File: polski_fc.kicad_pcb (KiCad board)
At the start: 8 copper layers, 37 x 37 mm, 157 parts, among them J2 JST-SH 1x08, J3 Digital_VTX_Connector, J4 UJ20-C-H-G-SMT-5-P16-TR, P1 4V5, P10 R1, P11 +, P12 C, P13 R5, P14 M1, P15 M2, P16 M3, P17 M4, P18 G, P19 5V, P2 G, P20 G, P21 VI, P22 5V, P23 G, P24 T5, P25 R5, P26 5V, P27 LED, P28 G, P29 5V, P3 SCL, P30 -B, P31 G, P32 T2, P33 R2, P34 R1, P35 G, P36 G, P37 9V, P38 5V, P39 G, P4 SDA, P40 5V, P41 G, P42 T5, P43 T5, P5 T3, P6 R3, P7 4V5, P8 G, P9 T1, Q1 NX138AKMYL, SW1 BOOT, U1 STM32G473RET6, U2 LMR33630CRNXR, U3 LMR33630CRNXR, U4 NCP187AMT330TAG, U5 TCR3RM33A, U6 ICM-42688-P, U7 DPS368XTSA1, U8 W25Q128JVPIQ, U9 STM32G431KBU6, Y1 8MHz

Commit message: Added silkscren
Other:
- board text added: "3V3"
- board text added: "4V5"
- board text added: "5V"
- board text added: "9V"
- board text added: "B-"
- board text added: "BAT"
- board text added: "CL"
- board text added: "CURR"
- board text added: "ESC"
- board text added: "G"
- board text added: "IMU"
- board text added: "IO"
- board text added: "L"
- board text added: "LED0"
- board text added: "M1"
- board text added: "M2"
- board text added: "M3"
- board text added: "M4"
- board text added: "MCU"
- board text added: "R1"
- board text added: "R2"
- board text added: "R3"
- board text added: "R5"
- board text added: "S1"
- board text added: "S2"
- board text added: "SBUS"
- board text added: "SCL"
- board text added: "SDA"
- board text added: "T1"
- board text added: "T2"
- board text added: "T3"
- board text added: "T5"
- board text added: "TELE"
- board text added: "VI"
- board text added: "VO"
- board text added: "VO/S"
- board text added: "VTX"

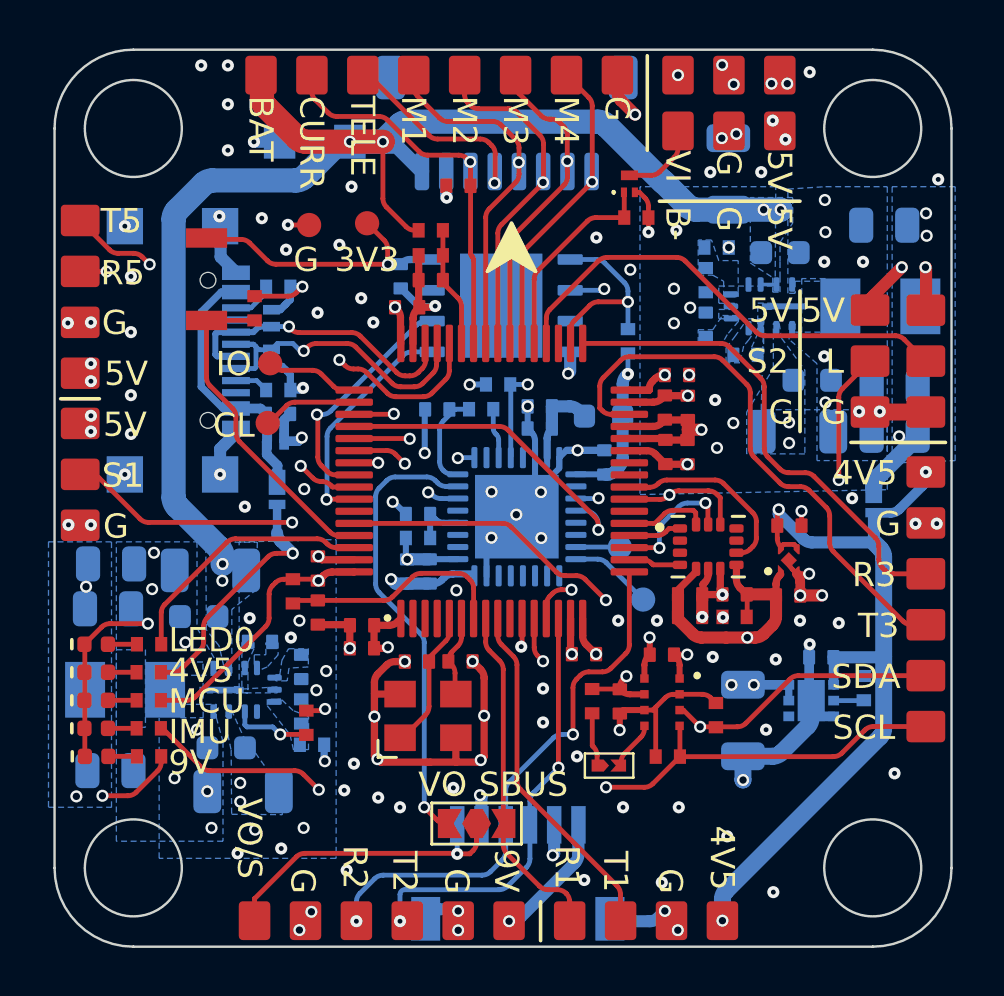
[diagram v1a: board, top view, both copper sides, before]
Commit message: Add return vias for SPI and fixed some rouding traces
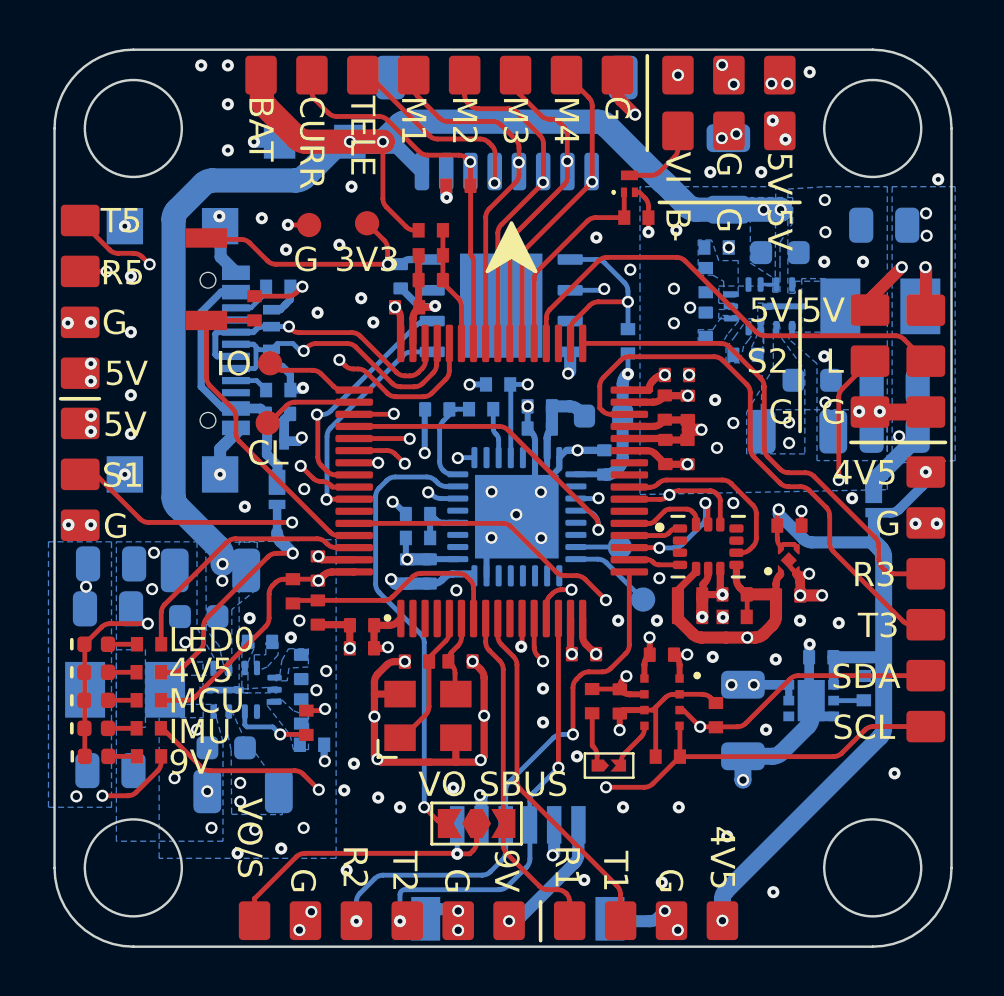
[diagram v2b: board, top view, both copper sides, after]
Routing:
- net /Project Architecture/IMU & Baro/GYRO_EXTI: track 1.58 -> 2.15 mm
- net GND: vias 146 -> 148

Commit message: Crystal change, gnd cut-out for crystal, bom update
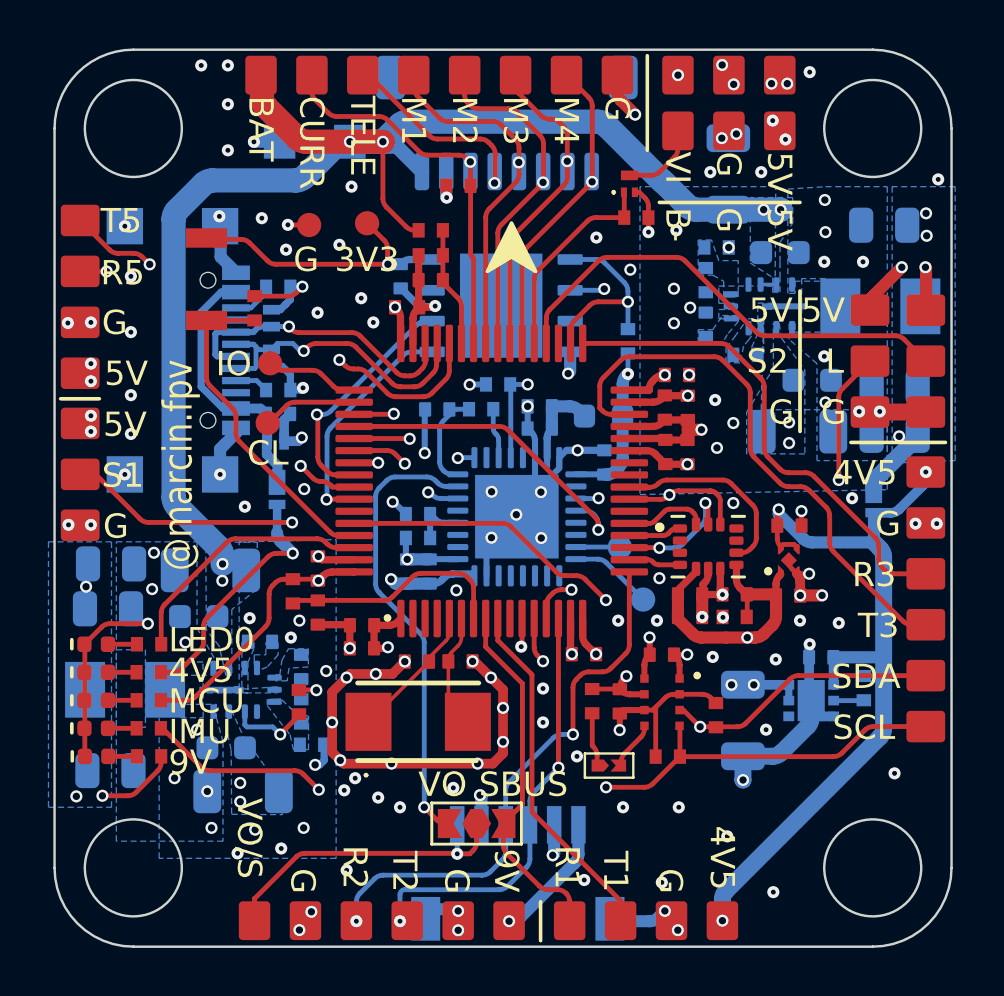
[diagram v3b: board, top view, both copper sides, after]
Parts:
- C7, C8: value 18p -> 24p
- Y1: footprint 0_passives:Crystal_SMD_3225-4Pin_3.2x2.5mm -> 0_passives:ABM3
- moved R35 0.90 mm to (133.5, 93.7)
- moved Y1 0.47 mm to (138.4, 94.5)
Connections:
- Y1 pad 2: GND -> /Project Architecture/MCU/MCU_OSC_OUT
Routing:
- net GND: track 107.0 -> 109.1 mm, vias 148 -> 152
- net /Project Architecture/IMU & Baro/BARO_I2C_SCL: track 38.8 -> 36.9 mm
- net /Project Architecture/MCU/MCU_OSC_OUT: track 3.13 -> 4.73 mm
- net /Project Architecture/MCU/VTX_EN: track 17.2 -> 18.2 mm
- net 9V: track 50.0 -> 50.9 mm
- net /Project Architecture/Interfaces/UART1_RX (RECV): track 14.9 -> 15.6 mm
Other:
- board text added: "@marcin.fpv"
